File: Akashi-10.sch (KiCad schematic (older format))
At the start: 7 parts, among them J1 Conn_02x20_Odd_Even, J2 Conn_02x20_Odd_Even, J3 Conn_02x20_Counter_Clockwise, P1 EL-210-KEY, U1 9-ST-20

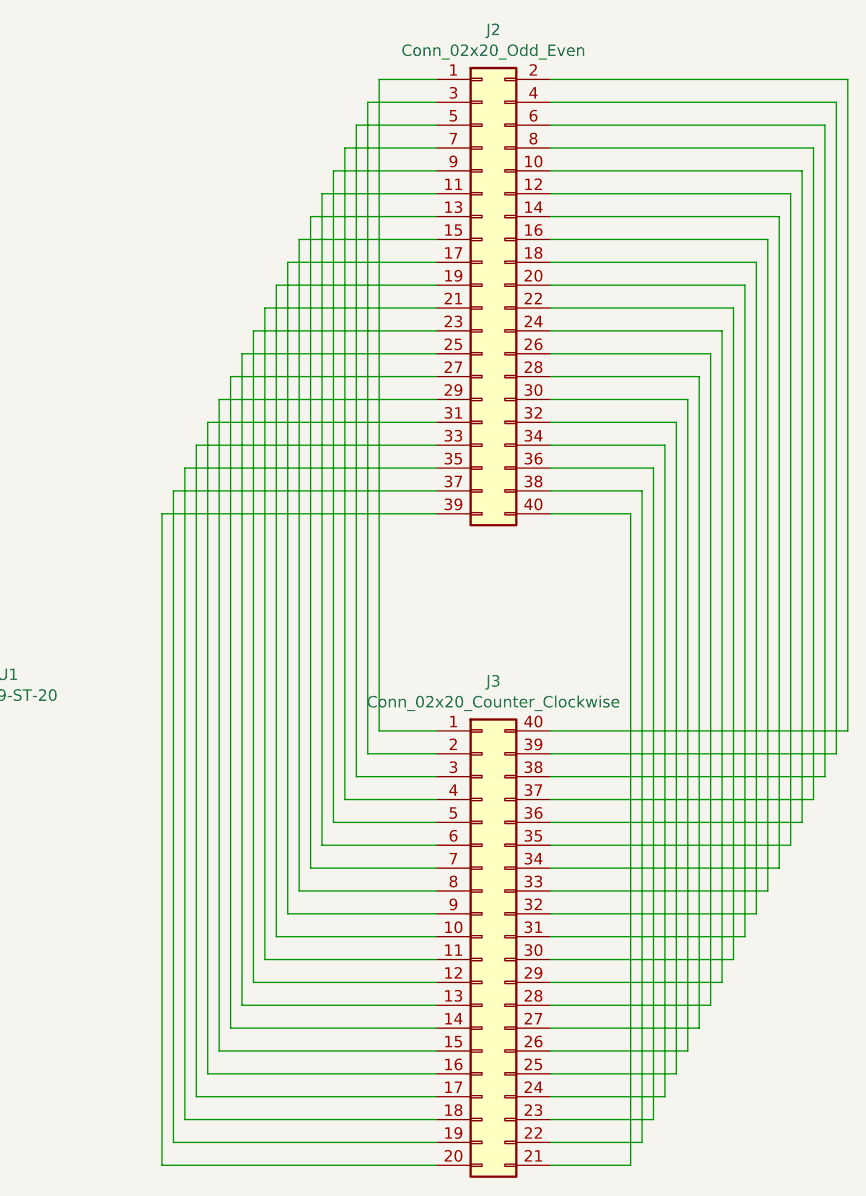
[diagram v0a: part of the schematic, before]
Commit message: Add lost holes.
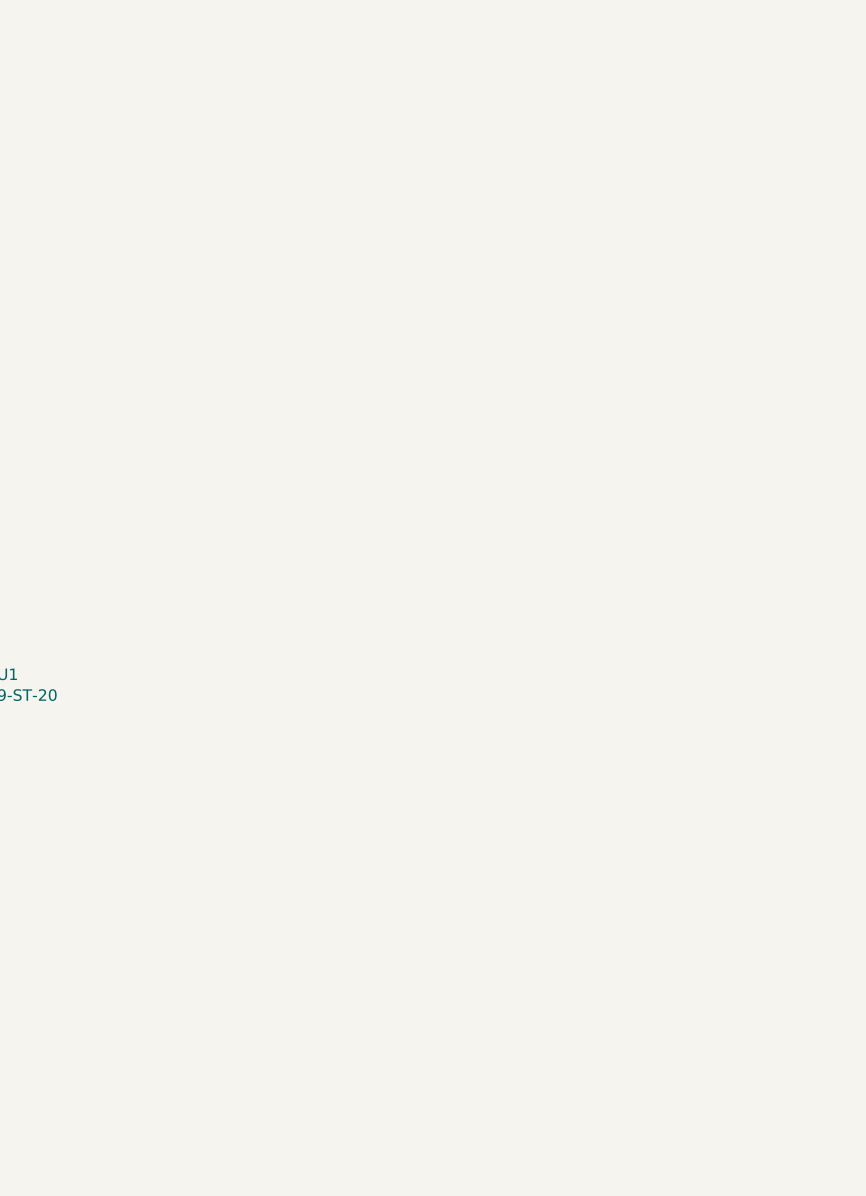
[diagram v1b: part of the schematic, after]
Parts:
- removed J2: Conn_02x20_Odd_Even, Connector_PinHeader_2.54mm:PinHeader_2x20_P2.54mm_Vertical, symbol Connector_Generic:Conn_02x20_Odd_Even
- removed J3: Conn_02x20_Counter_Clockwise, Package_DIP:DIP-40_W15.24mm_Socket, symbol Connector_Generic:Conn_02x20_Counter_Clockwise

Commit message: Apply library modification to board.
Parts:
- added C1, C3: CP, symbol Device:CP
- added C2: C, symbol Device:C
- added D1: D_Schottky, symbol Device:D_Schottky
- added L1: L, symbol Device:L
- added R1, R2: R, symbol Device:R
- added TP3: TestPoint, symbol Connector:TestPoint
- added U2: LM27313XMF, Package_TO_SOT_SMD:SOT-23-5, symbol Regulator_Switching:LM27313XMF
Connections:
- net +3V3: now also C1.1, L1.1, U2.4 (EN), U2.5 (VIN)
- net GND: now also C1.2, C3.2, R2.2
- new net: D1.2 (A), L1.2, U2.1 (SW)
- new net: C2.2, R1.2, R2.1, U2.3 (FB)
- new net: C2.1, C3.1, D1.1 (K), R1.1, TP3.1
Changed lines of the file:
@@
 	-1   0    0    -1
 $EndComp
+$Comp
+L Regulator_Switching:LM27313XMF U2
+U 1 1 62CD07C5
+P 8950 3500
+F 0 "U2" H 8950 3867 50  0000 C CNN
+F 1 "LM27313XMF" H 8950 3776 50  0000 C CNN
+F 2 "Package_TO_SOT_SMD:SOT-23-5" H 9000 3250 50  0001 L CIN
+F 3 "http://www.ti.com/lit/ds/symlink/lm27313.pdf" H 8950 3600 50  0001 C CNN
+	1    8950 3500
+	1    0    0    -1
+$EndComp
+$Comp
+L Device:R R1
+U 1 1 62CD286A
+P 10250 3600
+F 0 "R1" H 10320 3646 50  0000 L CNN
+F 1 "R" H 10320 3555 50  0000 L CNN
+F 2 "" V 10180 3600 50  0001 C CNN
+F 3 "~" H 10250 3600 50  0001 C CNN
+	1    10250 3600
+	1    0    0    -1
+$EndComp
+$Comp
+L Device:R R2
+U 1 1 62CD307C
+P 10250 4100
+F 0 "R2" H 10320 4146 50  0000 L CNN
+F 1 "R" H 10320 4055 50  0000 L CNN
+F 2 "" V 10180 4100 50  0001 C CNN
+F 3 "~" H 10250 4100 50  0001 C CNN
+	1    10250 4100
+	1    0    0    -1
+$EndComp
+Wire Wire Line
+	8650 3400 8650 3600
+Wire Wire Line
+	8650 3400 8500 3400
+Connection ~ 8650 3400
+Wire Wire Line
+	10250 3750 10250 3850
+Wire Wire Line
+	10250 3450 10250 3400
+Wire Wire Line
+	10250 3400 10550 3400
+$Comp
+L Device:C C2
+U 1 1 62CE18BF
+P 9950 3600
+F 0 "C2" H 10065 3646 50  0000 L CNN
+F 1 "C" H 10065 3555 50  0000 L CNN
+F 2 "" H 9988 3450 50  0001 C CNN
+F 3 "~" H 9950 3600 50  0001 C CNN
+	1    9950 3600
+	1    0    0    -1
+$EndComp
+$Comp
+L Device:CP C3
+U 1 1 62CE230A
+P 10550 3850
+F 0 "C3" H 10668 3896 50  0000 L CNN
+F 1 "CP" H 10668 3805 50  0000 L CNN
+F 2 "" H 10588 3700 50  0001 C CNN
+F 3 "~" H 10550 3850 50  0001 C CNN
+	1    10550 3850
+	1    0    0    -1
+$EndComp
+$Comp
+L Device:D_Schottky D1
+U 1 1 62CEAA9A
+P 9600 3400
+F 0 "D1" H 9600 3183 50  0000 C CNN
+F 1 "D_Schottky" H 9600 3274 50  0000 C CNN
+F 2 "" H 9600 3400 50  0001 C CNN
+F 3 "~" H 9600 3400 50  0001 C CNN
+	1    9600 3400
+	-1   0    0    1
+$EndComp
+$Comp
+L Device:L L1
+U 1 1 62CEB8E0
+P 8950 2950
+F 0 "L1" V 9140 2950 50  0000 C CNN
+F 1 "L" V 9049 2950 50  0000 C CNN
+F 2 "" H 8950 2950 50  0001 C CNN
+F 3 "~" H 8950 2950 50  0001 C CNN
+	1    8950 2950
+	0    -1   -1   0
+$EndComp
+$Comp
+L Device:CP C1
+U 1 1 62CEC29C
+P 8250 3850
+F 0 "C1" H 8368 3896 50  0000 L CNN
+F 1 "CP" H 8368 3805 50  0000 L CNN
+F 2 "" H 8288 3700 50  0001 C CNN
+F 3 "~" H 8250 3850 50  0001 C CNN
+	1    8250 3850
+	1    0    0    -1
+$EndComp
+Wire Wire Line
+	9750 3400 9950 3400
+Connection ~ 10250 3400
+Wire Wire Line
+	9950 3450 9950 3400
+Connection ~ 9950 3400
+Wire Wire Line
+	9950 3400 10250 3400
+Wire Wire Line
+	9450 3400 9350 3400
+Wire Wire Line
+	9950 3750 9950 3850
+Wire Wire Line
+	9950 3850 10250 3850
+Connection ~ 10250 3850
+Wire Wire Line
+	10250 3850 10250 3950
+Wire Wire Line
+	10550 3700 10550 3400
+Connection ~ 10550 3400
+Wire Wire Line
+	8250 3700 8250 3400
+Connection ~ 8250 3400
+Wire Wire Line
+	8250 4000 8250 4400
+Wire Wire Line
+	10250 4250 10250 4400
+Wire Wire Line
+	10550 4000 10550 4400
+$Comp
+L power:GND #PWR08
+U 1 1 62CFED41
+P 10550 4400
+F 0 "#PWR08" H 10550 4150 50  0001 C CNN
+F 1 "GND" H 10555 4227 50  0000 C CNN
+F 2 "" H 10550 4400 50  0001 C CNN
+F 3 "" H 10550 4400 50  0001 C CNN
+	1    10550 4400
+	1    0    0    -1
+$EndComp
+$Comp
+L power:GND #PWR07
+U 1 1 62CFF282
+P 10250 4400
+F 0 "#PWR07" H 10250 4150 50  0001 C CNN
+F 1 "GND" H 10255 4227 50  0000 C CNN
+F 2 "" H 10250 4400 50  0001 C CNN
+F 3 "" H 10250 4400 50  0001 C CNN
+	1    10250 4400
+	1    0    0    -1
+$EndComp
+$Comp
+L power:GND #PWR06
+U 1 1 62CFF64F
+P 8250 4400
+F 0 "#PWR06" H 8250 4150 50  0001 C CNN
+F 1 "GND" H 8255 4227 50  0000 C CNN
+F 2 "" H 8250 4400 50  0001 C CNN
+F 3 "" H 8250 4400 50  0001 C CNN
+	1    8250 4400
+	1    0    0    -1
+$EndComp
+Wire Wire Line
+	9950 3850 9550 3850
+Wire Wire Line
+	9550 3850 9550 3600
+Wire Wire Line
+	9550 3600 9250 3600
+Connection ~ 9950 3850
+Wire Wire Line
+	9350 3400 9350 2950
+Wire Wire Line
+	9350 2950 9100 2950
+Connection ~ 9350 3400
+Wire Wire Line
+	9350 3400 9250 3400
+Wire Wire Line
+	8800 2950 8500 2950
+Wire Wire Line
+	8500 2950 8500 3400
+Connection ~ 8500 3400
+Wire Wire Line
+	8500 3400 8250 3400
+Wire Wire Line
+	10550 3400 10800 3400
+Wire Wire Line
+	8000 3400 8250 3400
+$Comp
+L power:+3.3V #PWR05
+U 1 1 62D172B6
+P 8000 3400
+F 0 "#PWR05" H 8000 3250 50  0001 C CNN
+F 1 "+3.3V" H 8015 3573 50  0000 C CNN
+F 2 "" H 8000 3400 50  0001 C CNN
+F 3 "" H 8000 3400 50  0001 C CNN
+	1    8000 3400
+	1    0    0    -1
+$EndComp
+$Comp
+L Connector:TestPoint TP3
+U 1 1 62D18A49
+P 10800 3400
+F 0 "TP3" H 10858 3518 50  0000 L CNN
+F 1 "TestPoint" H 10858 3427 50  0000 L CNN
+F 2 "" H 11000 3400 50  0001 C CNN
+F 3 "~" H 11000 3400 50  0001 C CNN
+	1    10800 3400
+	1    0    0    -1
+$EndComp
 $EndSCHEMATC
